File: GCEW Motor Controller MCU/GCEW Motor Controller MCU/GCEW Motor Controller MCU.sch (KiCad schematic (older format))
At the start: 9 parts, among them J1 POWER IN, J2 MC2, J3 MC1, J4 Programmer, U1 ATmega328PB-AU, U2 HC-05_BluetoothModule

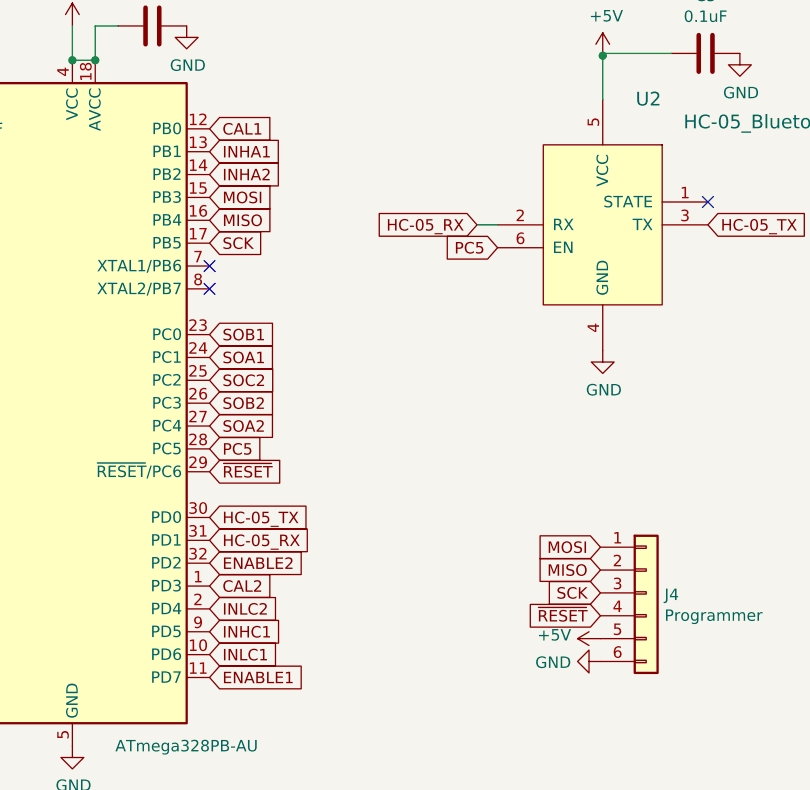
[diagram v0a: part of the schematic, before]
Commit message: GCEW Motor Controller MCU PCB Update 1
Finished PCB track layout. Need to finish adding text to bottom silkscreen layer.
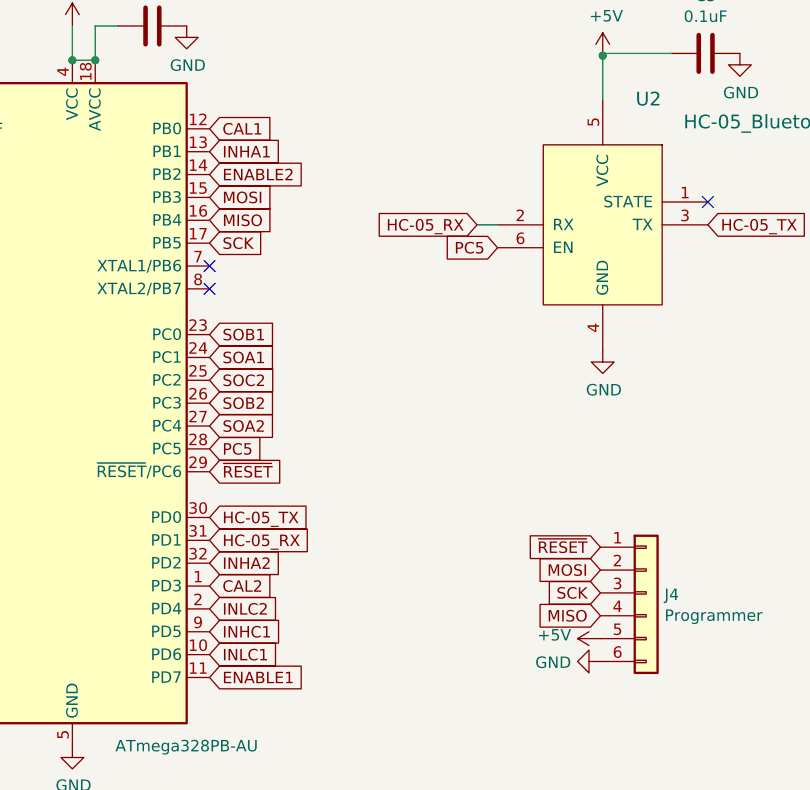
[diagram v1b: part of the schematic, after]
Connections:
- net ENABLE2: now also U1.14 (PB2); no longer U1.32 (PD2)
- net INHA2: now also U1.32 (PD2); no longer U1.14 (PB2)
- net MISO: now also J4.4 (Pin_4); no longer J4.2 (Pin_2)
- net MOSI: now also J4.2 (Pin_2); no longer J4.1 (Pin_1)
- net ~RESET: now also J4.1 (Pin_1); no longer J4.4 (Pin_4)
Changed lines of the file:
@@
 	1    0    0    -1
 $EndComp
-Text GLabel 7660 3580 0    50   Input ~ 0
+Text GLabel 7660 3680 0    50   Input ~ 0
 MOSI
-Text GLabel 7660 3680 0    50   Input ~ 0
+Text GLabel 7660 3880 0    50   Input ~ 0
 MISO
 Text GLabel 7660 3780 0    50   Input ~ 0
 SCK
-Text GLabel 7660 3880 0    50   Input ~ 0
+Text GLabel 7660 3580 0    50   Input ~ 0
 ~RESET
 $Comp
@@
 Text GLabel 5950 1850 2    50   Input ~ 0
 INHA1
-Text GLabel 5950 1950 2    50   Input ~ 0
+Text GLabel 5950 3650 2    50   Input ~ 0
 INHA2
 Text GLabel 5950 3950 2    50   Input ~ 0
@@
 Text GLabel 5950 4150 2    50   Input ~ 0
 ENABLE1
-Text GLabel 5950 3650 2    50   Input ~ 0
+Text GLabel 5950 1950 2    50   Input ~ 0
 ENABLE2
 $Comp
